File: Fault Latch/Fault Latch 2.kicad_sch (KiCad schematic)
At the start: 113 parts, among them J1 1053141312, J3 1053131202, J4 1053131202, J5 1053131202, K3 Fujitsu_FTR-LYCA005x, K5 Fujitsu_FTR-LYCA005x, K6 Fujitsu_FTR-LYCA005x, Q101 Q_NPN_BEC, Q102 Q_NPN_BEC, Q103 Q_NPN_BEC, Q104 Q_NPN_BEC, Q105 Q_NMOS_GSD, Q106 Q_NMOS_GSD, Q110 Q_NPN_BEC, Q111 Q_NPN_BEC, Q112 Q_NMOS_GSD, Q113 Q_NMOS_GSD, Q114 Q_NMOS_GSD, Q115 Q_NMOS_GSD, Q117 Q_NMOS_GSD, Q118 Q_NMOS_GSD, Q119 Q_NMOS_GSD, Q120 Q_NMOS_GSD, Q121 Q_NMOS_GSD, Q122 Q_NMOS_GSD, Q123 Q_NMOS_GSD, Q124 Q_NMOS_GSD, Q125 Q_NMOS_GSD, SW101 SW_Omron_B3FS, SW102 SW_Omron_B3FS, SW103 SW_Omron_B3FS, U1 74LS279, U104 74AHC1G00, U109 74AHC1G00, U112 74AHC1G00, U117 74AHC1G00, U118 LM555xM, U2 LM1117DT-5.0, U3 TestPoint, U7 SN74AHC1G08DBVR, U8 SN74AHC1G08DBVR

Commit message: Fault Latch Finished Schematic V4
Finished revised schematic and started on layout.
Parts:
- removed C102, C119, C120: 100n, Capacitor_SMD:C_0603_1608Metric_Pad1.08x0.95mm_HandSolder, symbol Device:C
- removed C110: 0.1u, Capacitor_SMD:C_0402_1005Metric, symbol Device:C
- removed J3, J5: 1053131202, Connector_Molex:Molex_Nano-Fit_105313-xx02_1x02_P2.50mm_Horizontal, symbol molex.2-pin:1053131202
- removed K3, K5, K6: Fujitsu_FTR-LYCA005x, Relay_THT:Relay_SPDT_Fujitsu_FTR-LYCA005x_FormC_Vertical, symbol Relay:Fujitsu_FTR-LYCA005x
- removed Q119, Q121, Q122, Q123, Q124, Q125: Q_NMOS_GSD, Package_TO_SOT_SMD:SOT-23, symbol Transistor_FET:Q_NMOS_GSD
- removed R106, R107, R109, R116, R126, R134: 1k, Resistor_SMD:R_1210_3225Metric, symbol Device:R_US
- removed R131: 15k, Resistor_SMD:R_1210_3225Metric, symbol Device:R_US
- removed R135: 510R, Resistor_SMD:R_1210_3225Metric, symbol Device:R_US
- removed R138, R139, R140: 10k, Resistor_SMD:R_1210_3225Metric, symbol Device:R_US
- removed U104, U109, U112, U117: 74AHC1G00, Package_TO_SOT_SMD:SOT-23-5, symbol 74xGxx:74AHC1G00
- removed U3: TestPoint, TestPoint:TestPoint_Pad_D1.5mm, symbol New_Library:BTS4141NHUMA1_
- added C1: 100n, Capacitor_SMD:C_0603_1608Metric_Pad1.08x0.95mm_HandSolder, symbol Device:C
- added C2, C3, C5, C6: 0.1u, Capacitor_SMD:C_0402_1005Metric, symbol Device:C
- added C4: 1u, Capacitor_SMD:C_0402_1005Metric, symbol Device:C_Polarized_US
- added D1, D2, D3: TVS Diode, Diode_SMD:Nexperia_DSN1608-2_1.6x0.8mm, symbol Diode:PTVS5V0Z1USK
- added IC1: CD4027BE, DIP794W53P254L1930H508Q16N, symbol 1.Custom:CD4027BE
- added J2: 4pinNanofit, Connector_Molex:Molex_Nano-Fit_105313-xx04_1x04_P2.50mm_Horizontal, symbol BSPD:SAMMY-4PIN
- added K1, K2, K3: Relay_SPDT_Omron_G2RL-1, Relay_THT:Relay_SPDT_Omron_G2RL-1, symbol Relay:G2RL-1
- added Q3, Q4: Q_NMOS_GSD, Package_TO_SOT_SMD:SOT-23, symbol Transistor_FET:Q_NMOS_GSD
- added R1, R12, R4, R7, R9: 10k, Resistor_SMD:R_1210_3225Metric, symbol Device:R_US
- added R10, R13: 510R, Resistor_SMD:R_1210_3225Metric, symbol Device:R_US
- added R141: 5.6k, Resistor_SMD:R_1210_3225Metric, symbol Device:R_US
- added R2, R6, R8: 1k, Resistor_SMD:R_1210_3225Metric, symbol Device:R_US
- added R3: 270R, Resistor_SMD:R_1210_3225Metric, symbol Device:R_US
- added R5: 2.2k, Resistor_SMD:R_1210_3225Metric, symbol Device:R_US
- added TP5, TP8, TP9: TestPoint, TestPoint:TestPoint_Pad_D1.5mm, symbol Connector:TestPoint
- added U3, U5, U6: SFH617A-1, Package_DIP:DIP-4_W7.62mm, symbol Isolator:SFH617A-1
- added U4: 74HC00, Package_DIP:DIP-14_W7.62mm, symbol 74xx:74HC00
- H101, H102, H103, H104: footprint MountingHole:MountingHole_3.2mm_M3 -> MountingHole:MountingHole_4.3mm_M4
- J1: footprint footprints:CONN_SD-105314-100_12_MOL -> 1.Custom:CONN_SD-105314-100_12_MOL_Nano
- U1: footprint Package_SO:SOIC-16_3.9x9.9mm_P1.27mm -> Package_DIP:DIP-16_W7.62mm
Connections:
- net NBMS_HV is gone; now on net Shutdown Circuit Out: J1.12
- net +12V: now also D104.1 (K), D108.1 (K), D110.1 (K), K1.A1, K2.A1, K3.A1, R12.1, R2.1; no longer J1.8, R112.1
- net +5V: now also C1.1, C4.1, C5.1, IC1.10 (J1), IC1.11 (K1), IC1.16 (VDD), R1.1, U3.4, U4.14 (VCC), U6.4; no longer D104.1 (K), D108.1 (K), D110.1 (K)
- net BMS_SR: now also U4.13
- net CLOCK: now also IC1.15 (Q1); no longer U118.3 (Q)
- net GND: now also J1.1, C1.2, C4.2, C5.2, D1.2 (A), D2.2 (A), D3.2 (A), IC1.12 (RESET1), IC1.3 (CLOCK2), IC1.4 (RESET2), IC1.5 (K2), IC1.6 (J2), IC1.7 (SET2), IC1.8 (VSS), IC1.9 (SET1), Q3.2 (S), Q4.2 (S), R3.1, R4.2, R5.2, R6.2, R7.2, R8.2, R9.2, U4.7 (GND), U5.3
- net IMD_SR: now also U4.12
- net NBMS_LV: now also R1.2, TP5.1, U4.1, U5.4
- net NBPSD_LV: now also R9.1, TP9.1, U3.3, U4.9
- net NIMD_LV: now also R4.1, TP8.1, U4.4, U6.3
- net NRESET_BMS: now also U4.2
- net NRESET_BSPD: now also U4.10
- net NRESET_IMD: now also U4.5
- net Shutdown Circuit In: now also J1.6, K1.14; no longer J4.1
- net Shutdown Circuit Out: now also K3.11; no longer J4.2
- net THRESH: now also R141.2
- net TSSI Green In: no longer J1.4
- net TSSI Green Out: no longer J1.3
- net TSSI Red Out: no longer J1.7
- net at TP4.1: now also K1.11, K2.14
- net at D104.2 (A), Q117.3 (D): now also K1.A2
- net BSPD_SR: now reaches D109.1 (K), Q120.1 (G), TP12.1, U1.9 (Q)
- net BSPD_SR: now also Q3.1 (G)
- net at D108.2 (A), Q118.3 (D): now also K2.A2
- net TSSI Green -: now reaches J1.9
- net at U7.1: now also U4.11
- net at U1.6 (~{S}): now also U4.6
- net at TP11.1: now also K2.11, K3.14
- net IMD Button -: now reaches R113.1, R114.2, SW102.1
- net IMD Button -: now also J2.3
- net at U1.11 (~{S}), U1.12 (~{S}): now also U4.8
- net at D110.2 (A), Q120.3 (D): now also K3.A2
- net at U1.2 (~{S}), U1.3 (~{S}): now also U4.3
- net BMS Button -: now reaches R101.1, R105.2, SW101.1
- net BMS Button -: now also J2.4
- net BSPD Button -: now reaches R122.1, R123.2, SW103.1
- net BSPD Button -: now also J2.2
- net BMS Light In renamed BMS
- net BMS: now also C2.1, D1.1 (K), R2.2, U5.1
- net BMS Light Out: no longer names the net of Q115.3 (D)
- net BMS Light Out: now also R10.2; no longer J1.1
- net BSPD_HV renamed IMD Light -
- net IMD Light -: now also R112.1
- net IMD Light In: no longer names the net of R112.2
- net IMD Light In: now also Q106.3 (D); no longer J1.6
- net IMD Light Out renamed BSPD Light -
- net BSPD Light -: now also R13.1; no longer Q106.3 (D)
- net IMD_HV: no longer names the net of J1.11
- new net: C6.2, R8.1, U3.2
- new net: C2.2, R3.2, U5.2
- new net: Q3.3 (D), Q4.1 (G), R12.2
- new net: Q4.3 (D), R13.2
- new net: C3.2, R6.1, U6.2
- new net: IC1.13 (CLOCK1), R141.1, U118.3 (Q)
- new net 12V Isolated +: J1.7
- new net 5V FL: J2.1
- new net BMS Light -: J1.4, R10.1
- new net BSPD: C6.1, D3.1 (K), J4.1, R7.1, U3.1
- new net IMD: C3.1, D2.1 (K), J1.8, R5.1, U6.1
- new net TSSI Red -: J1.3
- no-connect marks 6 -> 12
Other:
- moved on the sheet: C107, C108, C109, C111, C112, C113, C114, C115, C116, C118, D102, D104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

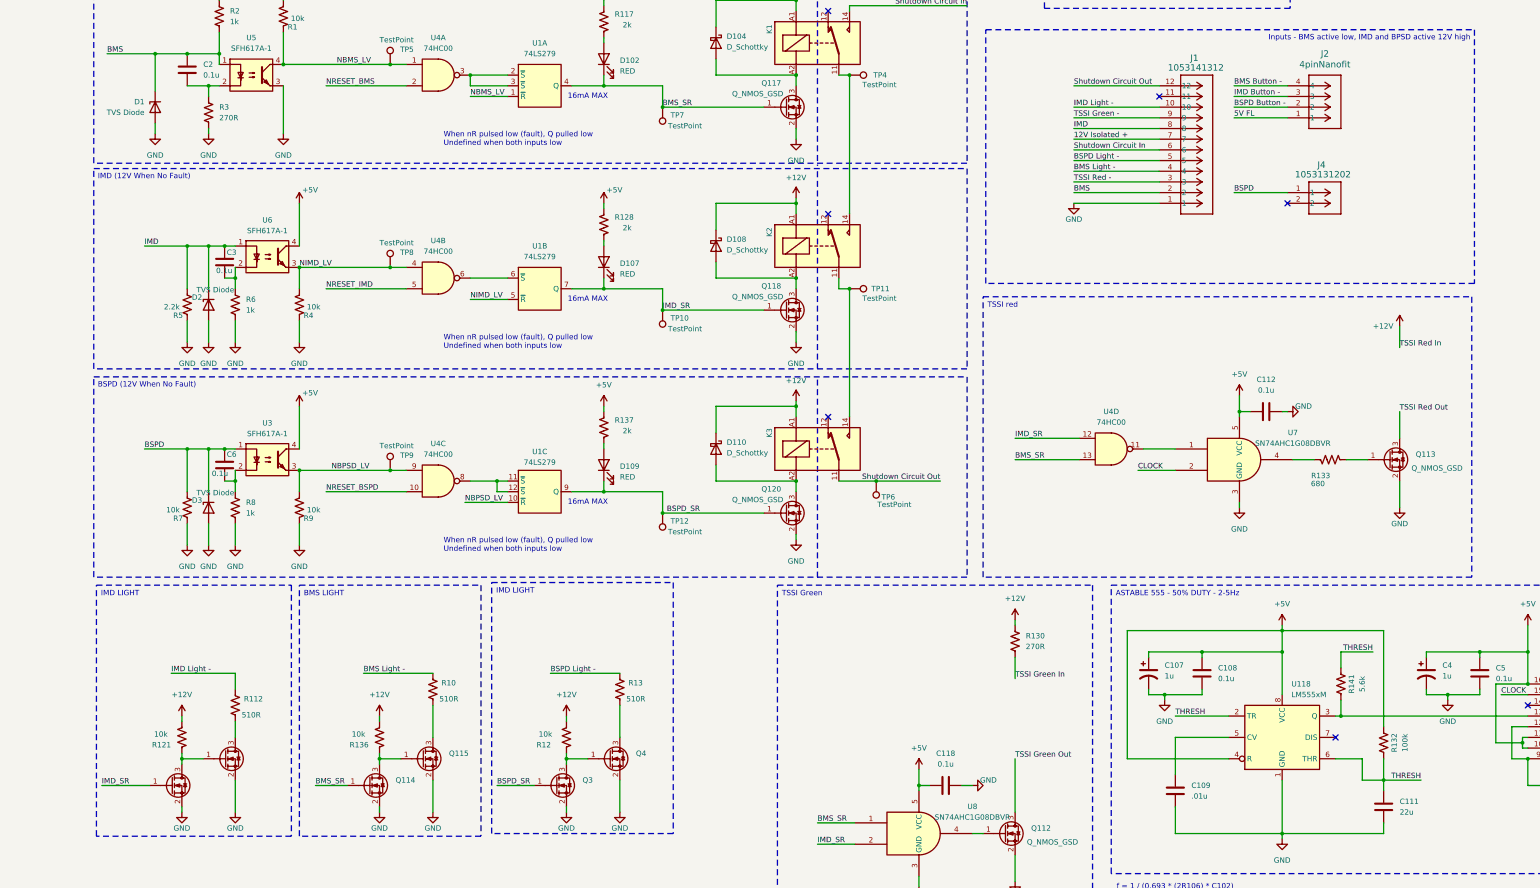
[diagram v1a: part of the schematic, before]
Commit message: Fault Latch V4 (almost RTO needs mounting holes)
Needs a final edge cut and mounting holes placed on it, besides that everything else is ready.
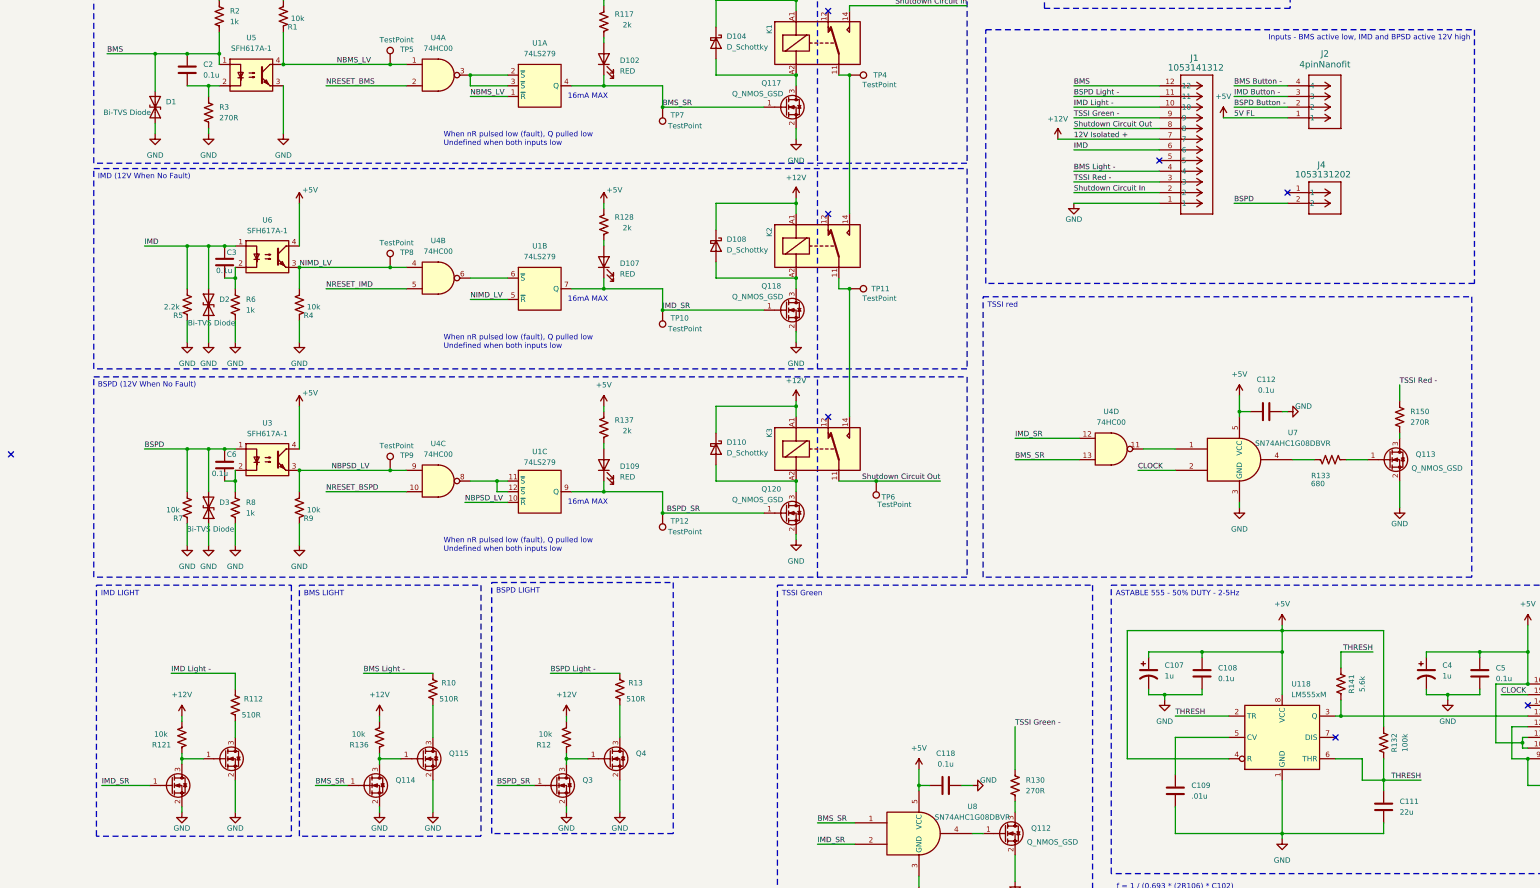
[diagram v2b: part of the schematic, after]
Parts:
- removed D1, D2, D3: TVS Diode, Diode_SMD:Nexperia_DSN1608-2_1.6x0.8mm, symbol Diode:PTVS5V0Z1USK
- added D1, D2, D3: Bi-TVS Diode, Diode_SMD:D_SOD-523, symbol Diode:ESD9B5.0ST5G
- added R150: 270R, Resistor_SMD:R_1210_3225Metric, symbol Device:R_US
- R5: footprint Resistor_SMD:R_1210_3225Metric -> Resistor_SMD:R_2512_6332Metric
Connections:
- net 12V Isolated + is gone; now on net +12V: J1.7
- net 5V FL is gone; now on net +5V: J2.1
- net TSSI Green Out is gone; now on an unnamed net: Q112.3 (D)
- net +12V: no longer R130.2
- net BMS: now also J1.12, D1.2 (A2); no longer J1.2
- net BSPD: now also J4.2, D3.2 (A2); no longer J4.1
- net BSPD Light -: now also J1.11; no longer J1.5
- net GND: now also D1.1 (A1), D2.1 (A1), D3.1 (A1)
- net IMD: now also J1.6, D2.2 (A2); no longer J1.8
- net Shutdown Circuit In: now also J1.2; no longer J1.6
- net Shutdown Circuit Out: now also J1.8; no longer J1.12
- net TSSI Green -: now also R130.2
- net TSSI Red -: now also R150.2
- net TSSI Green In: no longer names the net of R130.1
- net TSSI Red Out: no longer names the net of Q113.3 (D)
- net TSSI Red Out: now also R150.1
- no-connect marks 12 -> 13
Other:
- moved on the sheet: R130

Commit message: Fault Latch RTO V4
Ready to order might push a different one with more sketches for final order.
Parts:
- H101, H102, H103, H104: footprint MountingHole:MountingHole_4.3mm_M4 -> MountingHole:MountingHole_4.3mm_M4_DIN965_Pad_TopOnly
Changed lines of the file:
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@@
 			)
 		)
-		(property "Footprint" "MountingHole:MountingHole_4.3mm_M4"
+		(property "Footprint" "MountingHole:MountingHole_4.3mm_M4_DIN965_Pad_TopOnly"
 			(at 278.765 74.295 0)
 			(effects
@@
 			)
 		)
-		(property "Footprint" "MountingHole:MountingHole_4.3mm_M4"
+		(property "Footprint" "MountingHole:MountingHole_4.3mm_M4_DIN965_Pad_TopOnly"
 			(at 253.365 74.295 0)
 			(effects
@@
 			)
 		)
-		(property "Footprint" "MountingHole:MountingHole_4.3mm_M4"
+		(property "Footprint" "MountingHole:MountingHole_4.3mm_M4_DIN965_Pad_TopOnly"
 			(at 278.765 65.405 0)
 			(effects
@@
 			)
 		)
-		(property "Footprint" "MountingHole:MountingHole_4.3mm_M4"
+		(property "Footprint" "MountingHole:MountingHole_4.3mm_M4_DIN965_Pad_TopOnly"
 			(at 253.365 65.405 0)
 			(effects

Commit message: FINAL RTO FL V4
Added tables for I/O and fixed some traces
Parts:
- U1: JLC# C556297 -> C41430933
- U4: DigiKey (none) -> 296-1563-5-ND; JLC# (none) -> C2902; MPN (none) -> SN74HC00N
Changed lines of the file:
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@@
 			)
 		)
+		(property "JLC#" "C2902"
+			(at 100.33 196.85 0)
+			(effects
+				(font
+					(size 1.27 1.27)
+				)
+				(hide yes)
+			)
+		)
+		(property "MPN" "SN74HC00N"
+			(at 100.33 196.85 0)
+			(effects
+				(font
+					(size 1.27 1.27)
+				)
+				(hide yes)
+			)
+		)
+		(property "DigiKey" "296-1563-5-ND"
+			(at 100.33 196.85 0)
+			(effects
+				(font
+					(size 1.27 1.27)
+				)
+				(hide yes)
+			)
+		)
 		(pin "3"
 		)
@@
 			)
 		)
+		(property "JLC#" "C2902"
+			(at 100.33 100.33 0)
+			(effects
+				(font
+					(size 1.27 1.27)
+				)
+				(hide yes)
+			)
+		)
+		(property "MPN" "SN74HC00N"
+			(at 100.33 100.33 0)
+			(effects
+				(font
+					(size 1.27 1.27)
+				)
+				(hide yes)
+			)
+		)
+		(property "DigiKey" "296-1563-5-ND"
+			(at 100.33 100.33 0)
+			(effects
+				(font
+					(size 1.27 1.27)
+				)
+				(hide yes)
+			)
+		)
 		(pin "3"
 		)
@@
 			)
 		)
-		(property "JLC#" "C556297"
+		(property "JLC#" " C41430933"
 			(at 124.46 151.13 0)
 			(effects
@@
 			)
 		)
-		(property "JLC#" "C556297"
+		(property "JLC#" " C41430933"
 			(at 441.96 35.56 0)
 			(effects
@@
 			)
 		)
-		(property "JLC#" "C556297"
+		(property "JLC#" " C41430933"
 			(at 124.46 102.87 0)
 			(effects
@@
 			)
 		)
-		(property "JLC#" "C556297"
+		(property "JLC#" " C41430933"
 			(at 491.49 59.69 0)
 			(effects
@@
 			)
 		)
+		(property "JLC#" "C2902"
+			(at 100.33 148.59 0)
+			(effects
+				(font
+					(size 1.27 1.27)
+				)
+				(hide yes)
+			)
+		)
+		(property "MPN" "SN74HC00N"
+			(at 100.33 148.59 0)
+			(effects
+				(font
+					(size 1.27 1.27)
+				)
+				(hide yes)
+			)
+		)
+		(property "DigiKey" "296-1563-5-ND"
+			(at 100.33 148.59 0)
+			(effects
+				(font
+					(size 1.27 1.27)
+				)
+				(hide yes)
+			)
+		)
 		(pin "3"
 		)
@@
 			)
 		)
-		(property "JLC#" "C556297"
+		(property "JLC#" " C41430933"
 			(at 124.46 199.39 0)
 			(effects
@@
 			)
 		)
+		(property "JLC#" "C2902"
+			(at 412.75 34.29 0)
+			(effects
+				(font
+					(size 1.27 1.27)
+				)
+				(hide yes)
+			)
+		)
+		(property "MPN" "SN74HC00N"
+			(at 412.75 34.29 0)
+			(effects
+				(font
+					(size 1.27 1.27)
+				)
+				(hide yes)
+			)
+		)
+		(property "DigiKey" "296-1563-5-ND"
+			(at 412.75 34.29 0)
+			(effects
+				(font
+					(size 1.27 1.27)
+				)
+				(hide yes)
+			)
+		)
 		(pin "3"
 		)
@@
 			(at 260.35 189.23 0)
 			(effects
+				(font
+					(size 1.27 1.27)
+				)
+				(hide yes)
+			)
+		)
+		(property "JLC#" "C2902"
+			(at 260.35 189.23 0)
+			(effects
+				(font
+					(size 1.27 1.27)
+				)
+				(hide yes)
+			)
+		)
+		(property "MPN" "SN74HC00N"
+			(at 260.35 189.23 0)
+			(effects
+				(font
+					(size 1.27 1.27)
+				)
+				(hide yes)
+			)
+		)
+		(property "DigiKey" "296-1563-5-ND"
+			(at 260.35 189.23 0)
+			(effects
